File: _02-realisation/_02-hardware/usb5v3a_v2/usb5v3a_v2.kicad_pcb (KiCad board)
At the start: 2 copper layers, 43.2 x 58.4 mm, 13 parts, among them J1 Conn_01x02_Male, J2 Conn_01x02_Male, U1 LM7805_TO220, U2 LM741, U3 INA219Module, U4 INA219Module, U5 OLED128x32

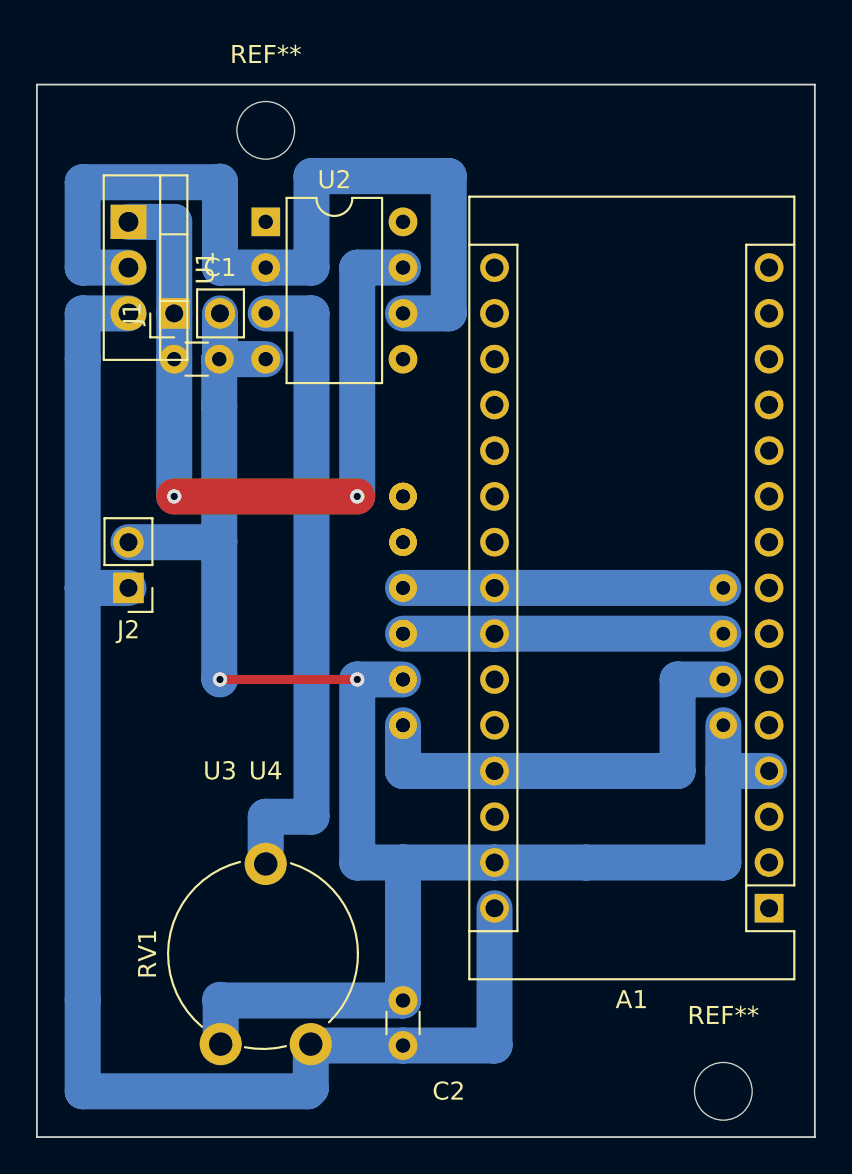
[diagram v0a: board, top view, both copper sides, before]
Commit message: USB 2x 3A v2 en cours (encoche PCB)
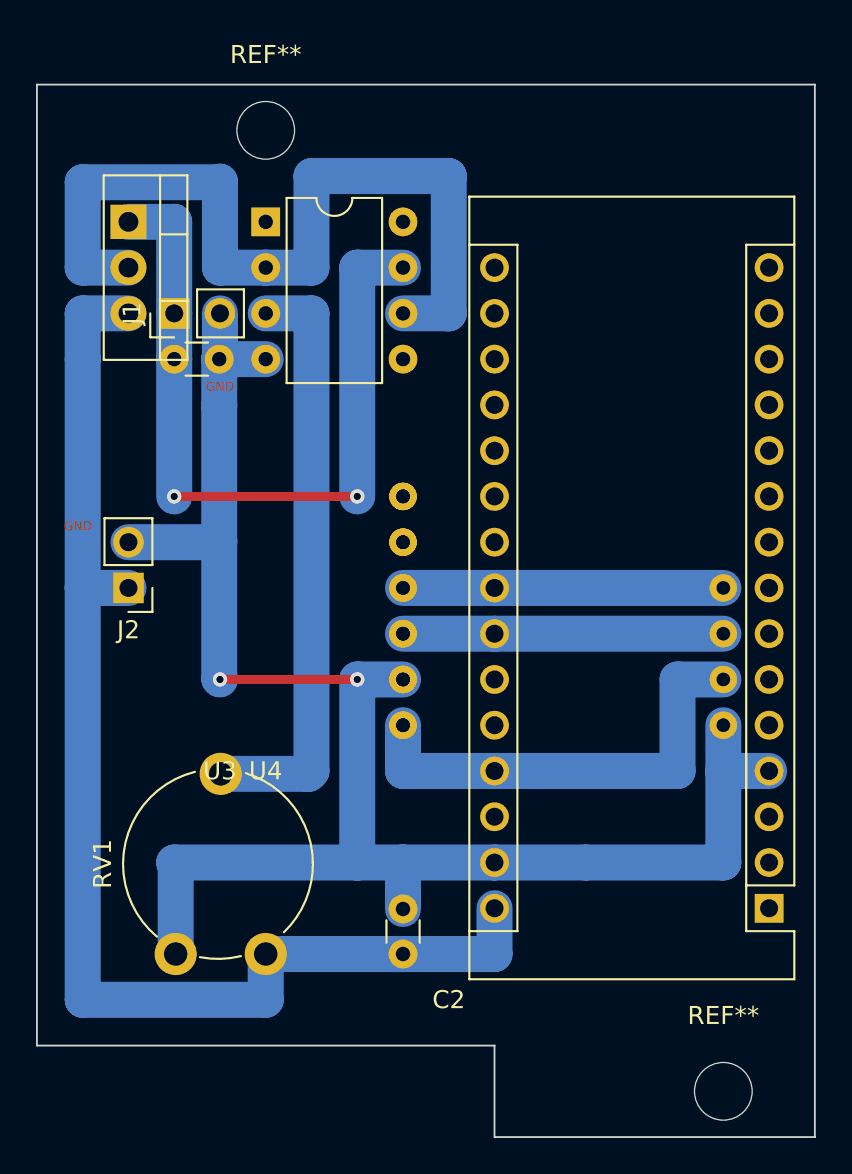
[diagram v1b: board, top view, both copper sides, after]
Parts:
- moved RV1 5.59 mm to (94.0, 86.4)
- moved C2 5.08 mm to (101.6, 86.4)
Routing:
- net +9V: track 81.3 -> 71.1 mm
- net Net-(RV1-Pad2): track 35.6 -> 33.0 mm
- net GND: track 99.0 -> 96.6 mm
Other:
- outline, holes or cut-outs redrawn
- board text added: "GND"
